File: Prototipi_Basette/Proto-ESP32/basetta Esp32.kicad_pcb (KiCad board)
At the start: 2 copper layers, 76.6 x 67.5 mm, 35 parts, among them J1 Conn_01x19, J2 Conn_01x19, J3 Conn_01x19, J4 Conn_01x19, J5 Screw_Terminal_01x02, J6 Conn_01x05, J7 Conn_01x02, J8 Conn_01x05, J9 Conn_01x05, Q1 BC557, Q2 BC547, Q3 BC547, Q4 BC547, Q5 IRF9540N, SW1 RESET, SW2 SET, U3 4013

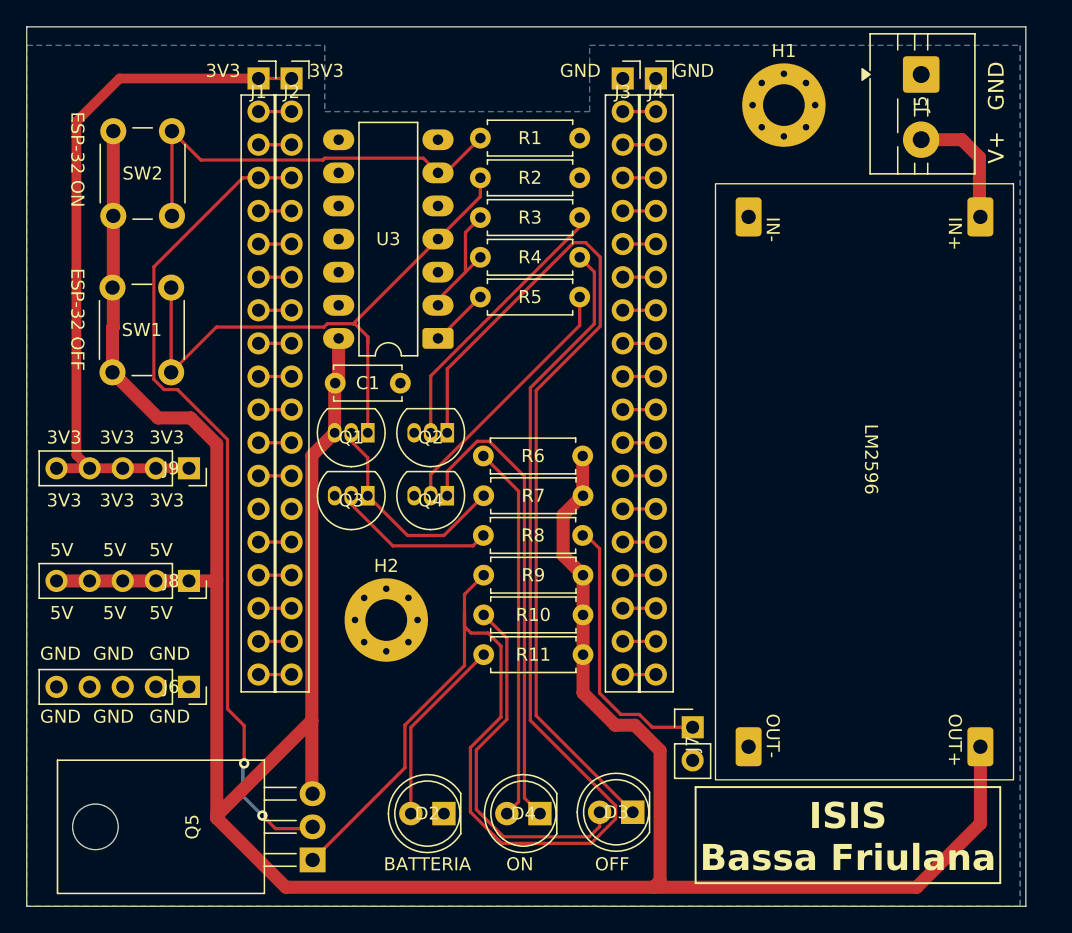
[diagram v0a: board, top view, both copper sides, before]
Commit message: Update ESP32 prototype files and add Gerbers
Remove obsolete Basetta_ESP32.zip and ITTCV-TDP-04 KiCad variant files; apply updates to the main KiCad project files (basetta Esp32.kicad_pcb, .kicad_prl, .kicad_pro, .kicad_sch). Add Gerber.zip with manufacturing outputs. Cleans up old artifacts and includes updated PCB/project metadata for the ESP32 prototype.
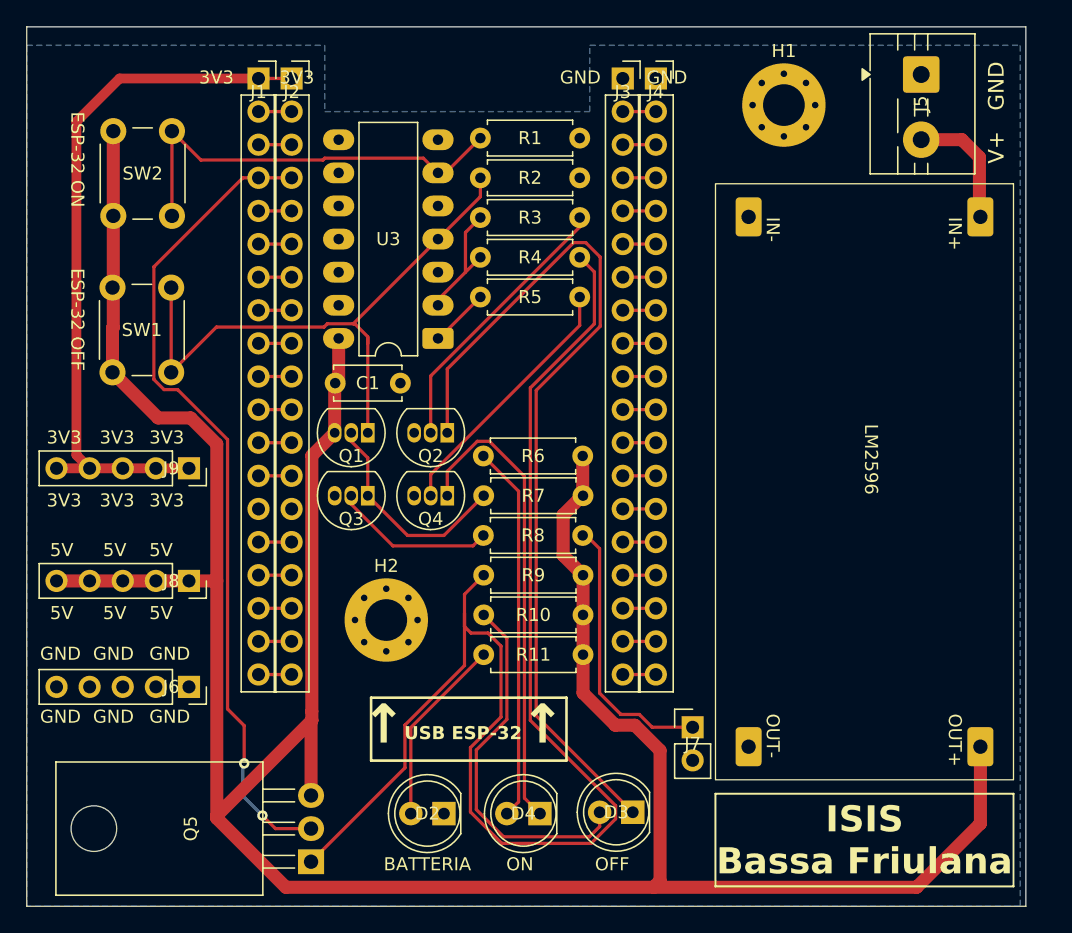
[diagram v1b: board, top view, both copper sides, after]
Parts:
- moved Q5 0.18 mm to (143.7, 121.0)
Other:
- board text added: "USB ESP-32"
- board text added: "↑"
- board text removed: "3V3"
- board text removed: "GND"
